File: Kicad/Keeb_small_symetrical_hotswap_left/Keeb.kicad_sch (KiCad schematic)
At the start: 32 parts, among them J1 TYPE-C-31-M-12, J2 B2B-XH-A_LF__SN_, SW1 CherryMX, SW10 CherryMX, SW11 CherryMX, SW13 CherryMX, SW14 CherryMX, SW15 CherryMX, SW16 CherryMX, SW17 CherryMX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

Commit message: Initial commit
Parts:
- removed J1: TYPE-C-31-M-12, TypeC:HRO_TYPE-C-31-M-12, symbol TypeC:TYPE-C-31-M-12
- removed SW2: CherryMX, ScottoKeebs_Hotswap:Hotswap_MX_Plated_1.00u_Smaller_hole, symbol Keeb-rescue:CherryMX-CherryMX
- removed U1: Pico, MCU_RaspberryPi_and_Boards:RPi_Pico_SMD_TH_NO_BACK_HOLES, symbol Keeb-rescue:Pico-MCU_RaspberryPi_and_Boards
- added J1: MJ-4PP-9_MJ-4PP-9, MJ-4PP-9:MJ-4PP-9, symbol Keeb-rescue:MJ-4PP-9-MJ-4PP-9
- added U3: nice_nano, Nice_nano:nice_nano, symbol nice_nano:nice_nano
- SW1, SW10, SW11, SW13, SW14, SW15, SW16, SW17, SW18, SW19, SW20, SW3, SW4, SW5, SW6, SW7, SW8, SW9: footprint ScottoKeebs_Hotswap:Hotswap_MX_Plated_1.00u_Smaller_hole -> ScottoKeebs_Hotswap:Hotswap_MX_Plated_1.00u
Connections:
- net 22 is gone; now on net 4: SW19.1
- net 26 is gone; now on net 3: SW20.1
- net 27 is gone; now on net 2: SW1.1
- net VSYS is gone; now on net 3v3: J2.1
- net 1: now also SW16.1, U3.1 (TX0/P0.06)
- net 10: now also U2.DT, U3.12 (P1.06); no longer SW8.2
- net 11: now also U2.CLK, U3.31 (P1.01); no longer SW9.1
- net 12: now also SW11.1, U3.32 (P1.02); no longer SW10.1
- net 13: now also SW10.1, U3.33 (P1.07); no longer SW11.1
- net 14: now also SW9.1, U3.13 (NFC1/P0.09)
- net 15: now also SW6.2, U3.14 (NFC2/P0.10)
- net 16: now also SW7.2, U3.15 (P1.11); no longer SW17.1
- net 17: now also SW8.2, U3.16 (P1.13); no longer SW18.1
- net 18: now also J1.3 (C), J1.4 (D), U3.17 (P1.15); no longer SW14.2
- net 19: now also SW3.2, U3.18 (AIN0/P0.02); no longer SW13.2
- net 2: now also U3.2 (RX1/P0.08)
- net 20: now also SW4.2, U3.19 (AIN5/P0.29); no longer SW16.1
- net 21: now also SW5.2, U3.20 (AIN7/P0.31); no longer SW15.2
- net 3: now also U3.5 (P0.17); no longer U2.DT
- net 3v3: now also J1.1 (A), U3.21 (VCC), U3.24 (BATIN/P0.04)
- net 4: now also U3.6 (P0.20); no longer U2.CLK
- net 5: now also SW15.2, U3.7 (P0.22); no longer SW5.2
- net 6: now also SW18.1, U3.8 (P0.24); no longer SW4.2
- net 7: now also SW14.1, U3.9 (P1.00); no longer SW3.2
- net 8: now also SW17.1, U3.10 (P0.11); no longer SW7.2
- net 9: now also SW13.1, U3.11 (P1.04); no longer SW6.2
- net GND: now also SW13.2, SW14.2, J1.2 (B), U3.23 (GND), U3.3 (GND), U3.4 (GND); no longer SW13.1, SW14.1
- net 28: no longer names the net of U2.SW
- new net RST: U3.22 (RST)

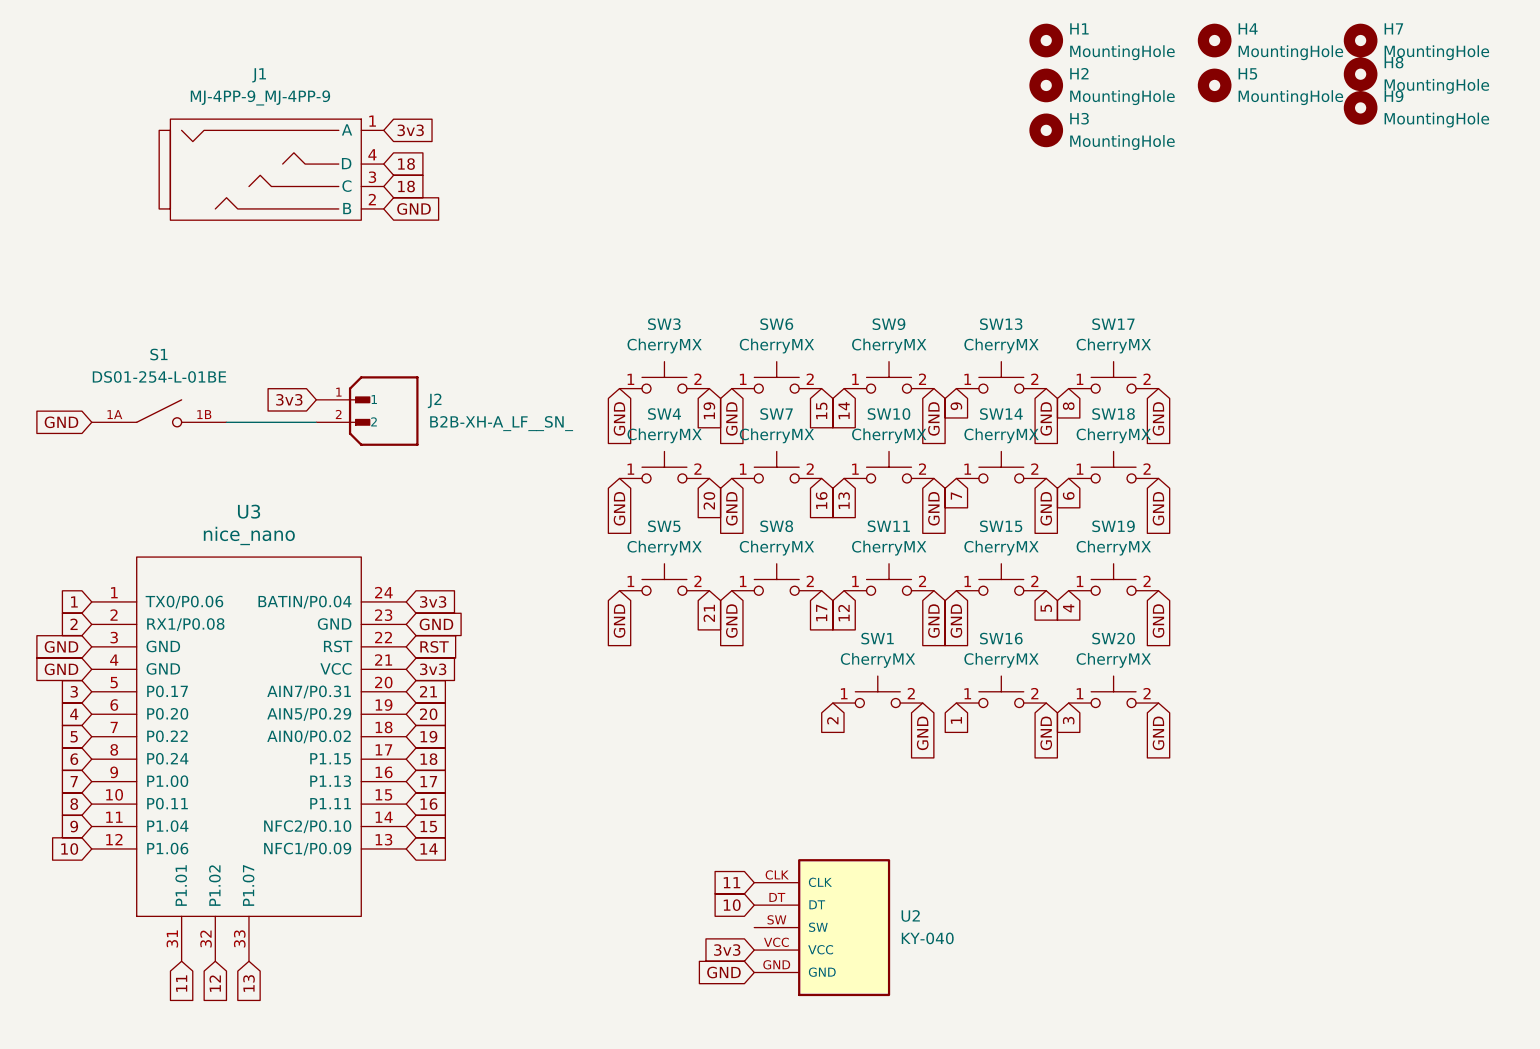
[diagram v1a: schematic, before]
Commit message: current version, all problems fixed, software compiled for CP 9.0
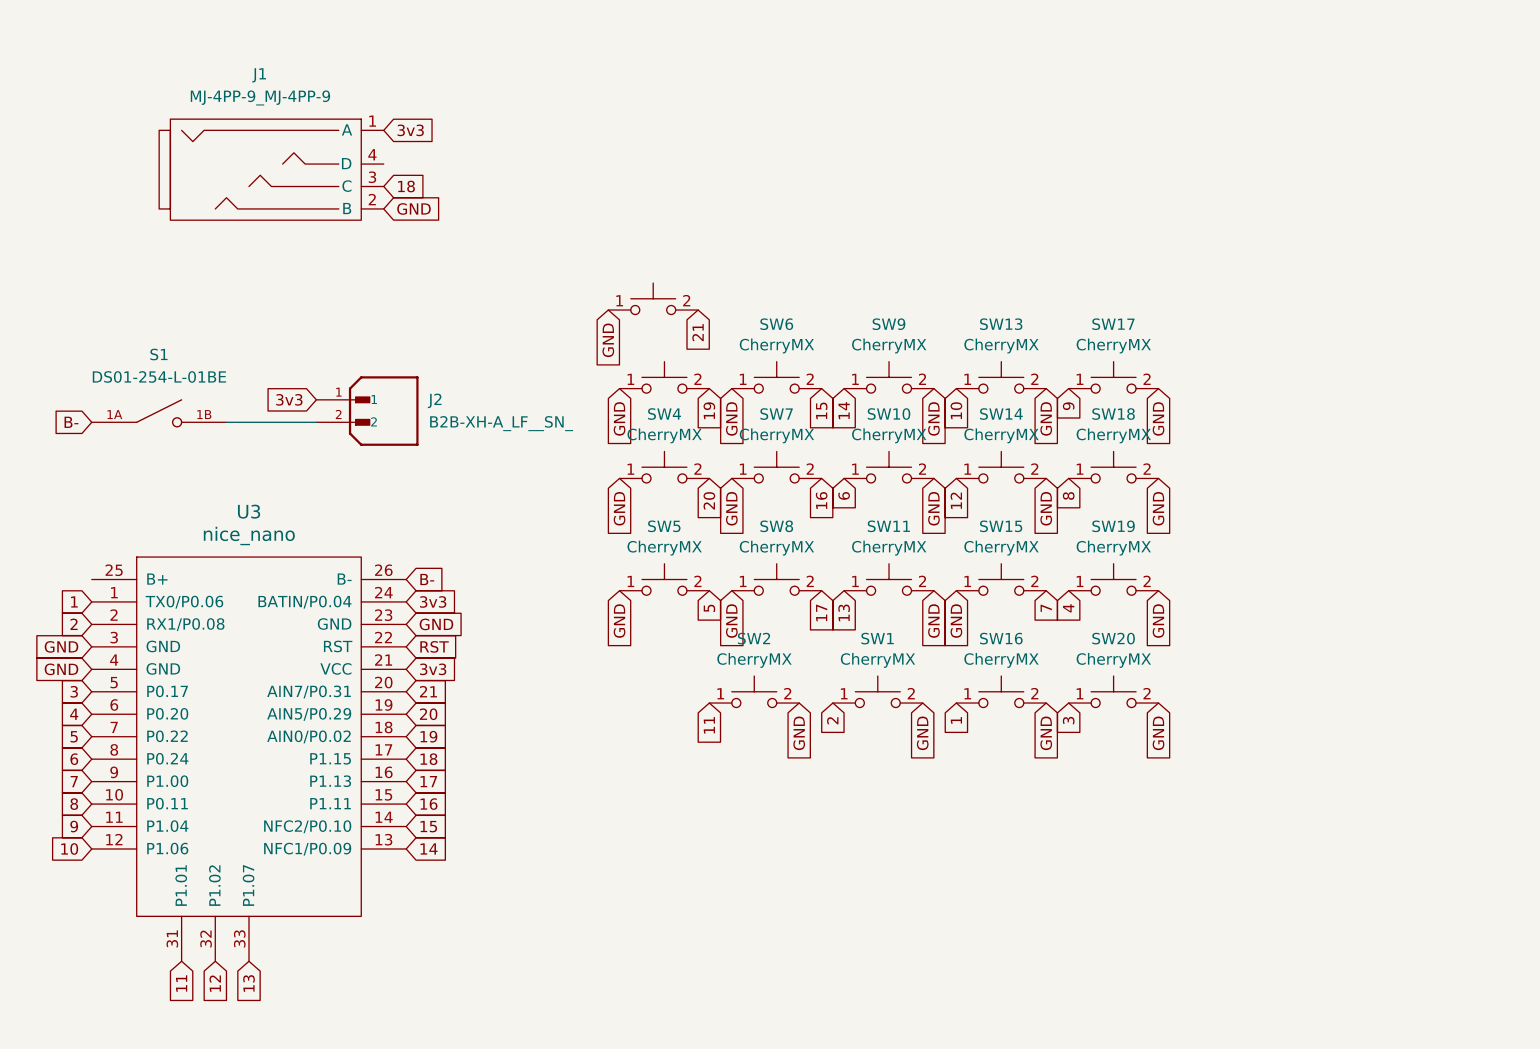
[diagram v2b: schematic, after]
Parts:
- removed H1, H2, H3, H4, H5, H7, H8, H9: MountingHole, MountingHole:MountingHole_3.2mm_M3, symbol Mechanical:MountingHole
- removed U2: KY-040, KY-040:KY-040-PORT, symbol KY-040:KY-040
- added SW12, SW2: CherryMX, ScottoKeebs_Hotswap:Hotswap_Choc_V1_Plated_1.00u, symbol Keeb-rescue:CherryMX-CherryMX
- SW1, SW10, SW11, SW13, SW14, SW15, SW16, SW17, SW18, SW19, SW20, SW3, SW4, SW5, SW6, SW7, SW8, SW9: footprint ScottoKeebs_Hotswap:Hotswap_MX_Plated_1.00u -> ScottoKeebs_Hotswap:Hotswap_Choc_V1_Plated_1.00u
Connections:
- net 10: now also SW13.1
- net 11: now also SW2.1
- net 12: now also SW14.1; no longer SW11.1
- net 13: now also SW11.1; no longer SW10.1
- net 18: no longer J1.4 (D)
- net 21: now also SW12.2; no longer SW5.2
- net 5: now also SW5.2; no longer SW15.2
- net 6: now also SW10.1; no longer SW18.1
- net 7: now also SW15.2; no longer SW14.1
- net 8: now also SW18.1; no longer SW17.1
- net 9: now also SW17.1; no longer SW13.1
- net GND: now also SW12.1, SW2.2; no longer S1.1A
- new net B-: S1.1A, U3.26 (B-)
